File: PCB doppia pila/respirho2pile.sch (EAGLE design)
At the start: 26 parts, among them U1 ICM-20948, U3 ADP1606ACPZN1.8-R7CP_6_3_ADI-L, X2 32.768kHz

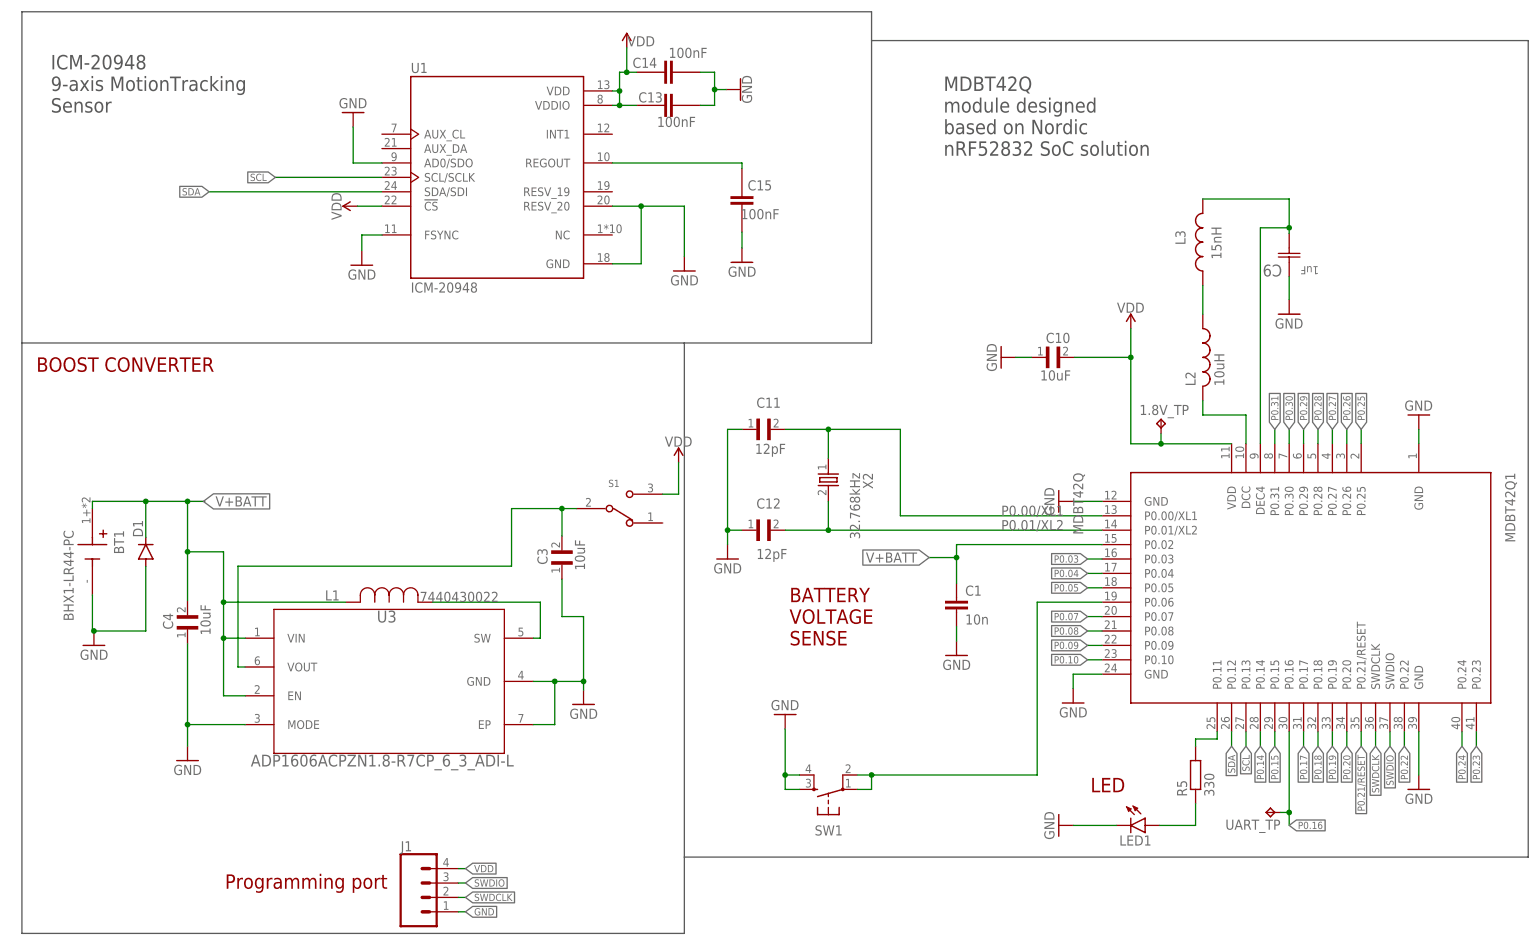
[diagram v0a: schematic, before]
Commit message: Aggiunte versioni con 2 pile
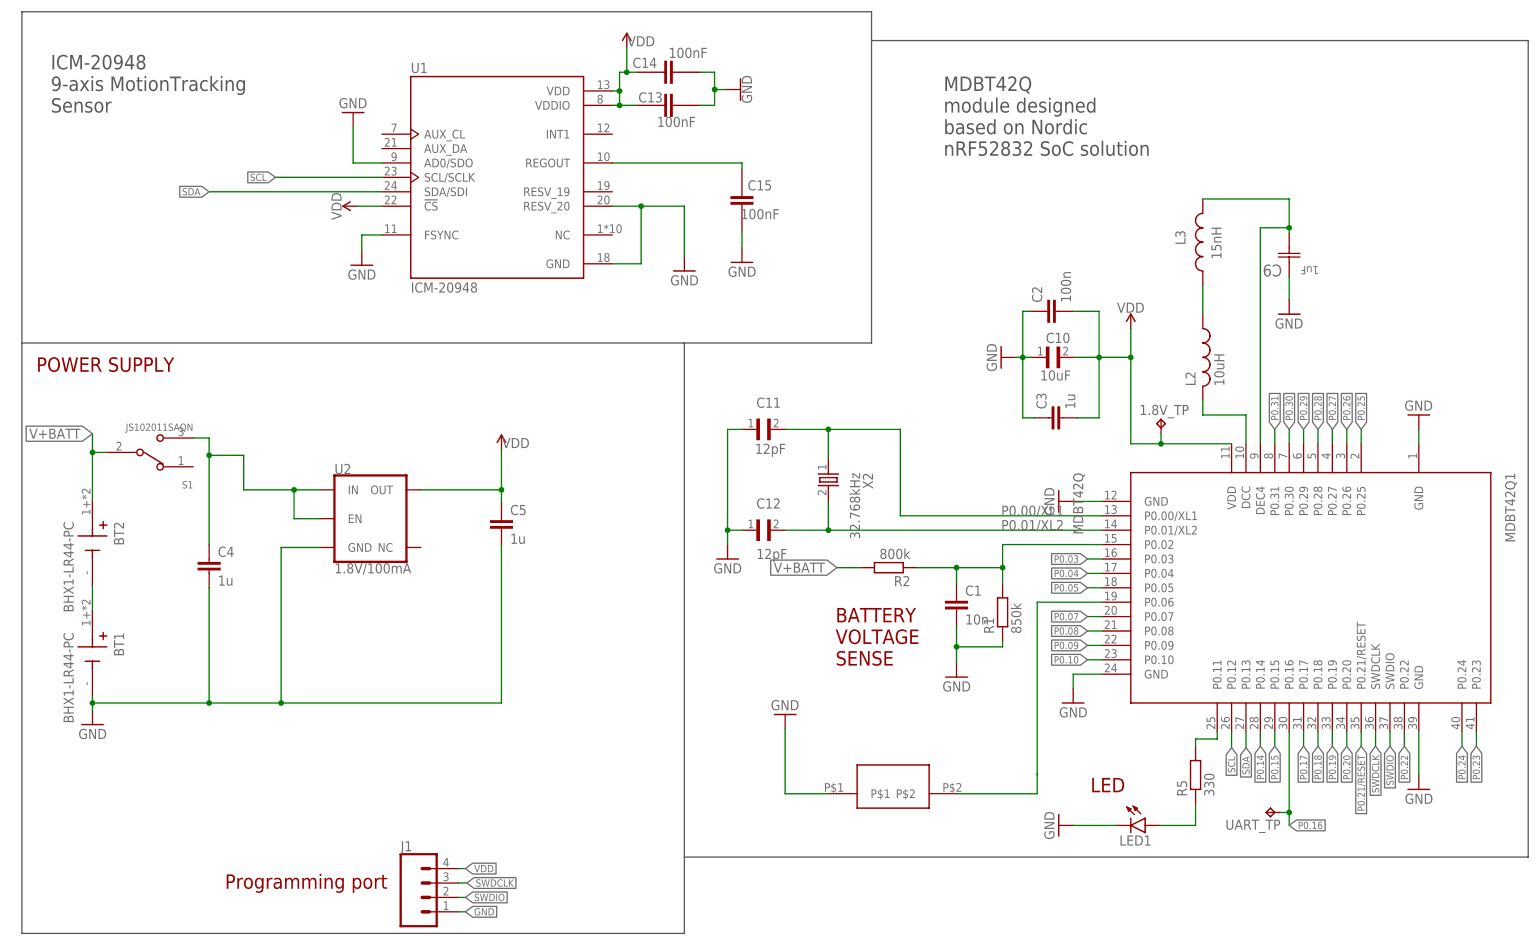
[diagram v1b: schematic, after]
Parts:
- removed D1: (no value), diode:DIODE-SOD323-R
- removed L1: 7440430022, inductor:7440430022
- removed SW1: (no value), SparkFun-Electromechanical:SWITCH_SPST_4_PINRECT
- removed U3: ADP1606ACPZN1.8-R7CP_6_3_ADI-L, AD1606:ADP1606ACPZN1.8-R7CP_6_3_ADI-L
- added BT2: BHX1-LR44-PC, BHX1-LR44-PC:BHX1-LR44-PC
- added C2: 100n, rcl:C-EUC0402
- added C5: 1u, rcl:C-EUC0402
- added R1: 850k, rcl:R-EU_R0603
- added R2: 800k, rcl:R-EU_R0603
- added U$1: KSS231GLFS, KSS231GLFS:KSS231GLFS
- added U2: 1.8V/100mA, SparkFun-IC-Power:V_REG_SP6214-1.8V
- C3: value 10uF -> 1u; device GRM188R61A106KE69J:GRM188R61A106KE69J -> rcl:C-EUC0603
- C4: value 10uF -> 1u; device GRM188R61A106KE69J:GRM188R61A106KE69J -> rcl:C-EUC0402
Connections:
- removed net IND: L1.1, U3.SW
- removed net VOUT: C3.2, S1.2, U3.VOUT
- new net N$6: BT1.+, BT2.-
- new net N$8: C4.1, S1.3, U2.EN, U2.IN
- new net N$9: C1.1, MDBT42Q1.P0.02, R1.2, R2.1
- net GND: now also C2.1, C4.2, C5.2, R1.1, U$1.P$1, U2.GND; no longer C4.1, D1.A, SW1.3, SW1.4, U3.EP, U3.GND, U3.MODE
- net P06: now also U$1.P$2; no longer SW1.1, SW1.2
- net SCL: now also MDBT42Q1.P0.12; no longer MDBT42Q1.P0.13
- net SDA: now also MDBT42Q1.P0.13; no longer MDBT42Q1.P0.12
- net SWDCLK: now also J1.3; no longer J1.2
- net SWDIO: now also J1.2; no longer J1.3
- net V+BATT: now also BT2.+, R2.2, S1.2; no longer BT1.+, C1.1, C4.2, D1.C, L1.2, MDBT42Q1.P0.02, U3.EN, U3.VIN
- net VDD: now also C2.2, C3.2, C5.1, U2.OUT; no longer S1.3
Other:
- note added: "POWER SUPPLY"
- note removed: "BOOST CONVERTER"
- moved on the sheet: BT1, C3, C4, S1

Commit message: Routing completo versione con 2 pile
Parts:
- removed C10: 10uF, GRM188R61A106KE69J:GRM188R61A106KE69J
- removed S1: JS102011SAQN, JS102011SAQN:JS102011SAQN
- added C6: 10u, rcl:C-EUC2012
- added SW1: EG1213, Slide_switch:EG1213
- C4, C5: device rcl:C-EUC0402 -> rcl:C-EUC0603
- R1: value 850k -> 866k
- R2: value 800k -> 806k
- U2: value 1.8V/100mA -> AP2127K-1.8V; device SparkFun-IC-Power:V_REG_SP6214-1.8V -> TPS7A05:TPS7A0518PDBVTK-1.8V
- renumbered R5 to R3, U$1 to SW2, X2 to X1
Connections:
- net GND: now also C4.1, C5.1, C6.1; no longer C10.1, C4.2, C5.2
- net N$8: now also C4.2, SW1.3; no longer C4.1, S1.3
- net SCL: now also MDBT42Q1.P0.13; no longer MDBT42Q1.P0.12
- net SDA: now also MDBT42Q1.P0.12; no longer MDBT42Q1.P0.13
- net V+BATT: now also SW1.2; no longer S1.2
- net VDD: now also C5.2, C6.2; no longer C10.2, C5.1
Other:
- note added: "BOOTLOADER BUTTON"
- moved on the sheet: C4, C5, U2

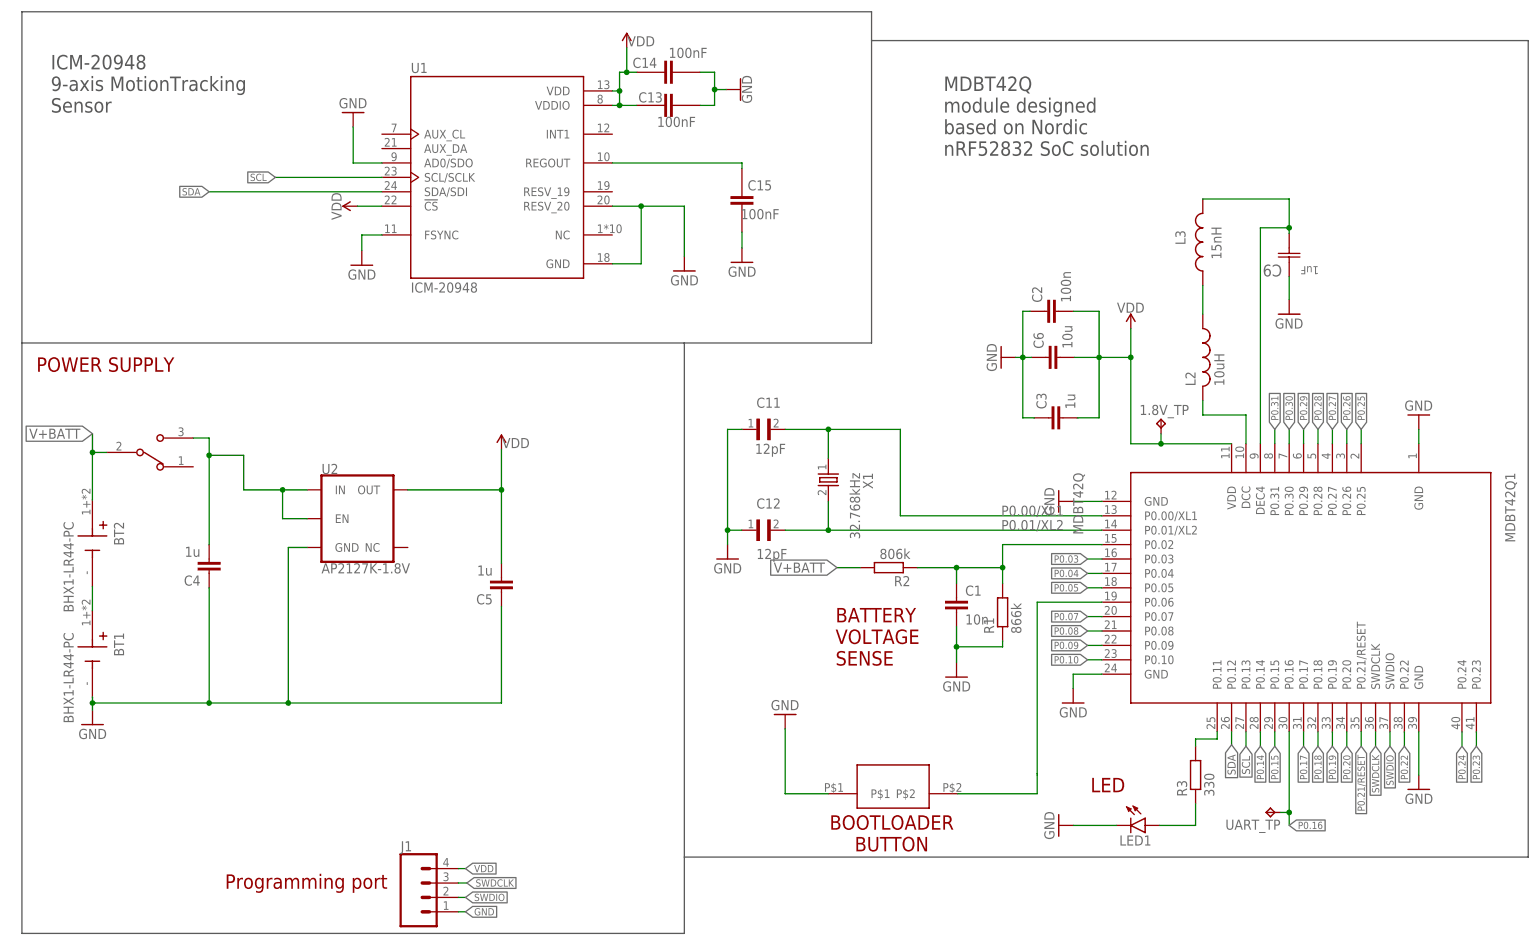
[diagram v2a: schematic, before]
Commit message: Cambiate delle footprint (R1,R2,R3) e altri piccoli miglioramenti
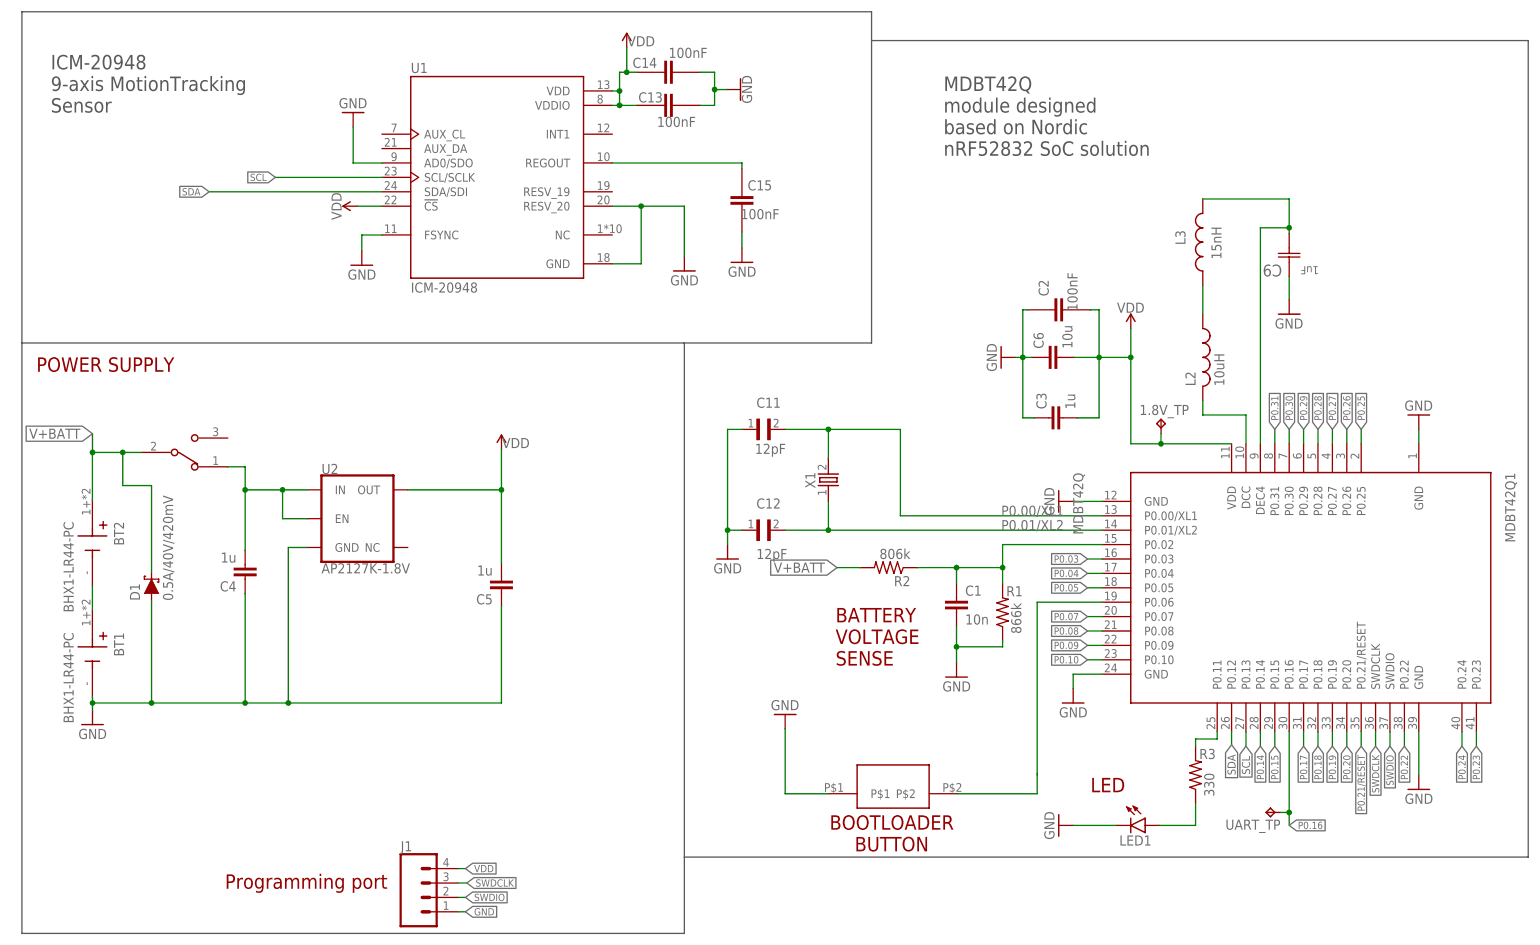
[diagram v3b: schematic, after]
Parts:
- added D1: 0.5A/40V/420mV, SparkFun-DiscreteSemi:DIODE-SCHOTTKY-PMEG4005EJ
- C2: value 100n -> 100nF; device rcl:C-EUC0402 -> CC0402KRX7R6BB104:CC0402KRX7R6BB104
- R1, R2, R3: device rcl:R-EU_R0603 -> rcl:R-US_R0402
- X1: value 32.768kHz -> (none); device Nordic_nRF:XTAL_32KHZ -> XTAL:XTAL_32KHZ
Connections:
- net GND: now also C2.2, D1.A; no longer C2.1
- net N$8: now also SW1.1; no longer SW1.3
- net P0.00/XL1: now also X1.2; no longer X1.1
- net P0.01/XL2: now also X1.1; no longer X1.2
- net V+BATT: now also D1.C
- net VDD: now also C2.1; no longer C2.2
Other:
- moved on the sheet: C4, X1

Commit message: Cambiate altre footprint e componenti non disponibili
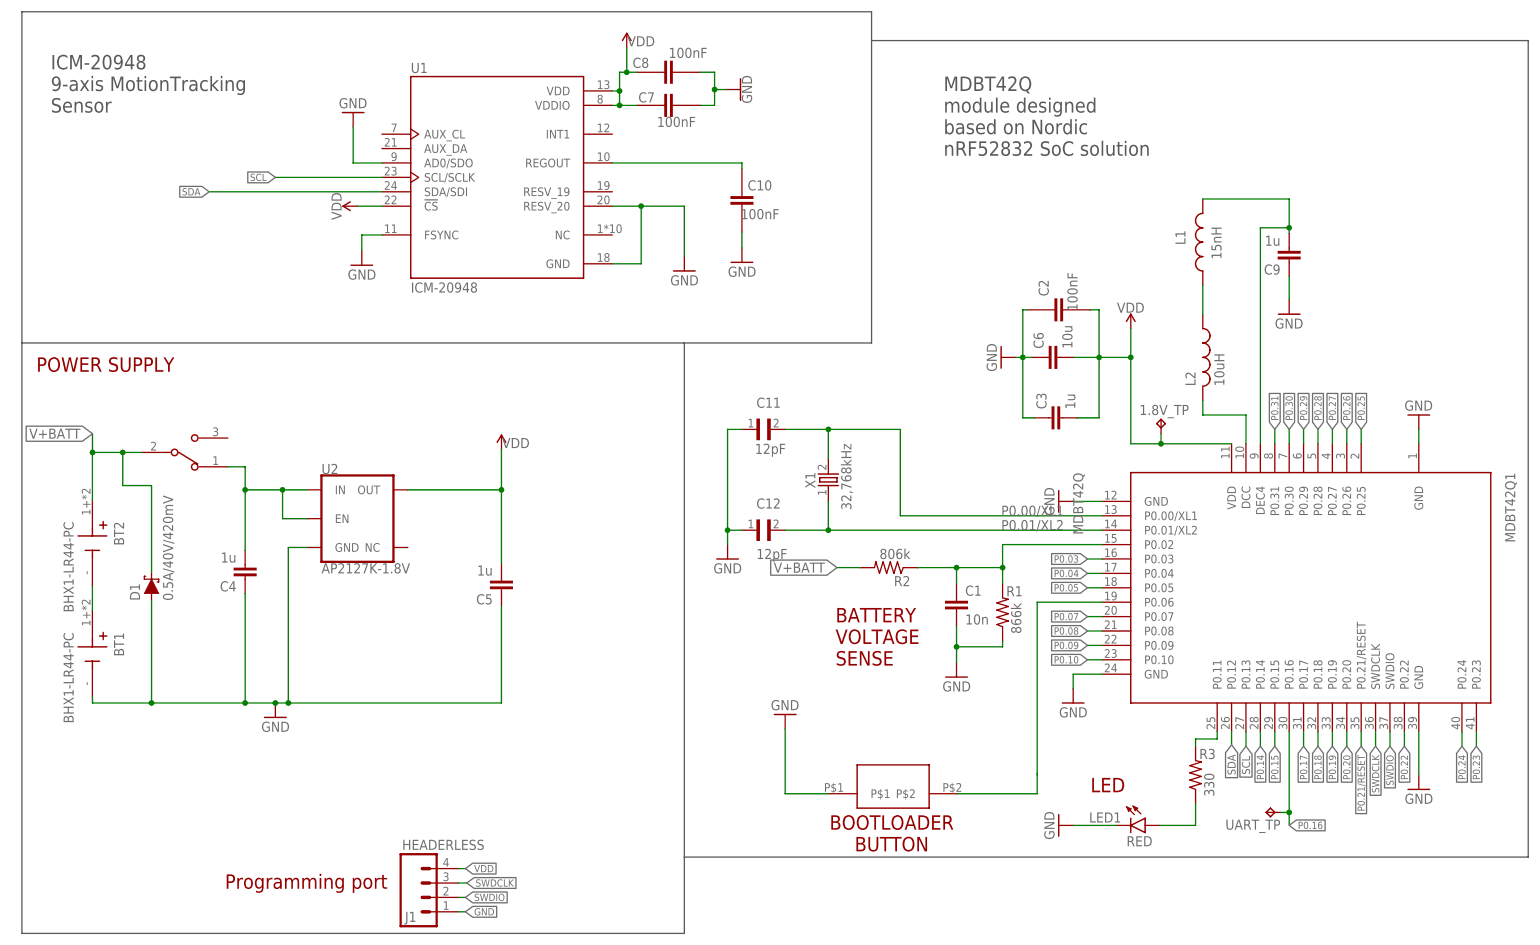
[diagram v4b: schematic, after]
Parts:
- C9: value 1uF -> 1u; device CC0603KRX7R7BB105:CC0603KRX7R7BB105 -> rcl:C-EUC0603
- J1: value (none) -> HEADERLESS
- LED1: value (none) -> RED
- X1: value (none) -> 32,768kHz
- renumbered C13 to C7, C14 to C8, C15 to C10, L3 to L1
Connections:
- net GND: now also C9.1; no longer C9.C1
- net N$4: now also C9.2; no longer C9.C2
